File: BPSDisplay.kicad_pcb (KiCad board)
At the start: 2 copper layers, 45 parts, among them J1 SWD, J2 Conn_02x06_Counter_Clockwise, P1 Conn_02x20_Odd_Even, SW1 Reset, U1 STM32F413RHTx, U7 NCP1117-3.3_SOT223, Y1 8M

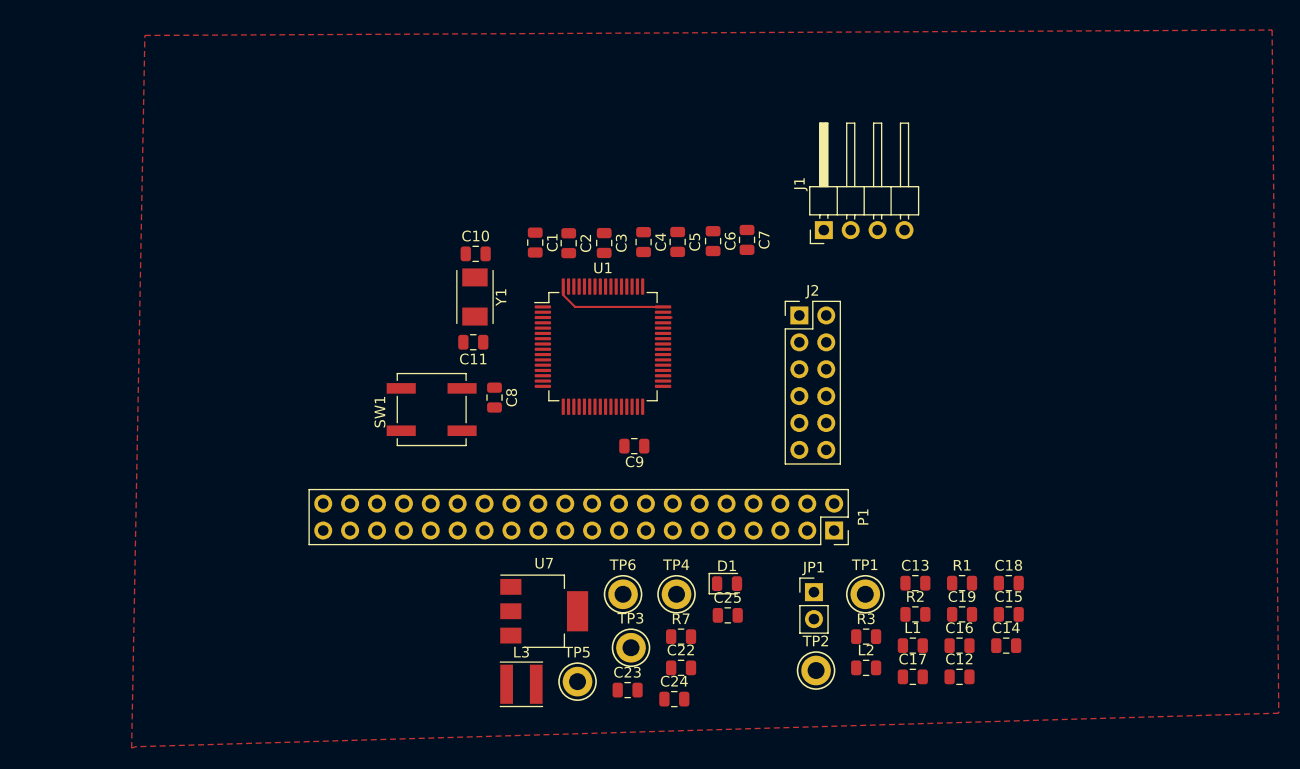
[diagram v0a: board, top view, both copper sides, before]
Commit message: Rearranging PCB layout
Power distribution circuit is laid out, CAN interface is done using the recommended PCB layout, and all the mounting holes and connectors are in the same places as they were in the old board.
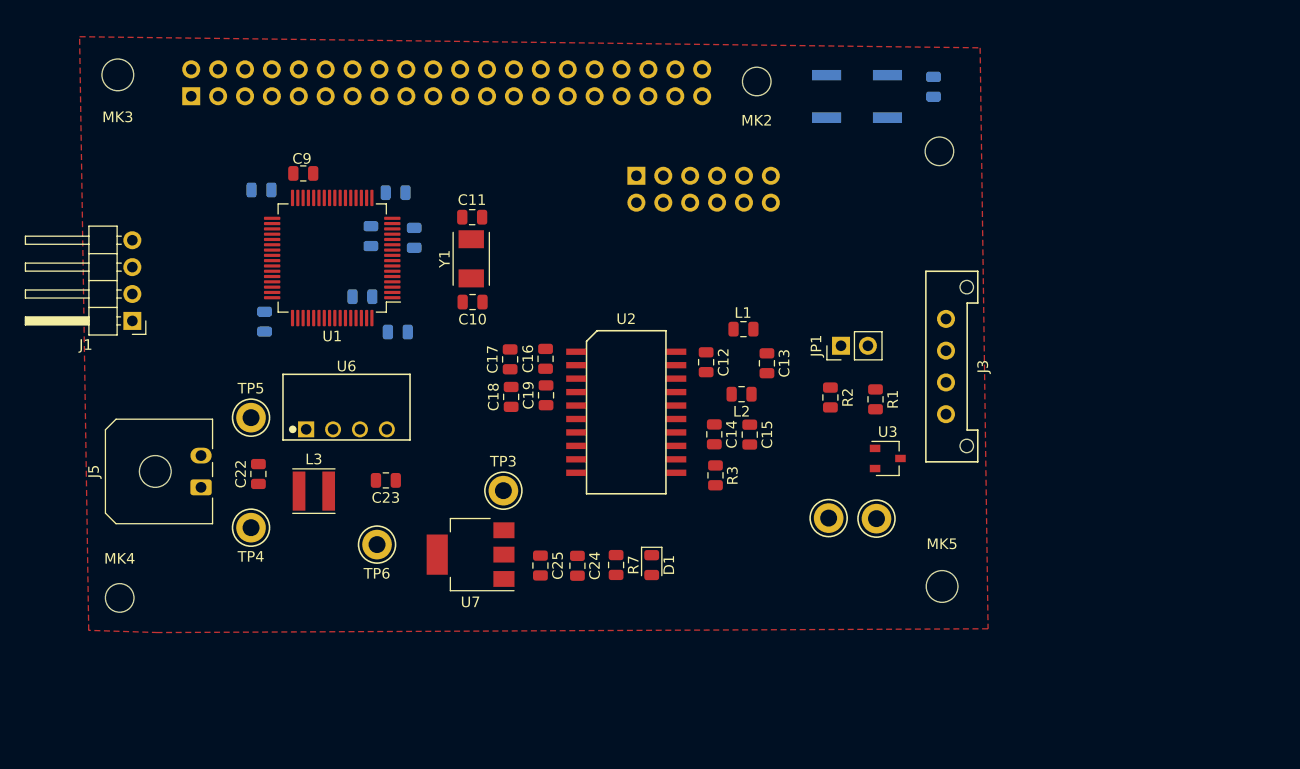
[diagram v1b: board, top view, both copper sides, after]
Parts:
- added J3: CAN_Out, UTSVT_Connectors:Molex_MicroFit3.0_1x4xP3.00mm_PolarizingPeg_Vertical, F.Cu at (278.0, 131.9)
- added J5: CarPowerConnector, Connector_Molex:Molex_Micro-Fit_3.0_43650-0200_1x02_P3.00mm_Horizontal, F.Cu at (207.6, 147.8)
- added MK1: M2.5, MountingHole:MountingHole_2.7mm_M2.5, F.Cu at (277.3, 116.0)
- added MK2: M2.5, MountingHole:MountingHole_2.7mm_M2.5, F.Cu at (260.1, 109.4)
- added MK3: M3, MountingHole:MountingHole_3mm, F.Cu at (199.7, 108.8)
- added MK4: M2.5, MountingHole:MountingHole_2.7mm_M2.5, F.Cu at (199.9, 158.2)
- added MK5: M3, MountingHole:MountingHole_3mm, F.Cu at (277.6, 157.1)
- added U2: ADM3055E, UTSVT_ICs:SOIC-20W_7.5x15.4mm_Pitch1.27mm, F.Cu at (247.8, 140.7)
- added U3: CDSOT23-T24CAN, Package_TO_SOT_SMD:SOT-23W, F.Cu at (272.5, 145.0)
- added U6: PDS1-S12-S5, UTSVT_ICs:PDSx-S, F.Cu at (221.3, 142.3)
- C1, C2, C3, C4, C5, C6, C7, C8, J2, P1, SW1: moved to B.Cu
- moved P1 73.3 mm to (206.7, 110.8)
- moved J1 65.9 mm to (201.1, 132.0), turned to 180 degrees
- moved C8 50.8 mm to (276.8, 109.9), turned to 90 degrees
- moved C18 50.2 mm to (236.9, 139.2), turned to 90 degrees
- moved SW1 49.9 mm to (269.6, 110.8)
- moved C17 48.4 mm to (236.8, 135.7), turned to 90 degrees
- moved C16 47.6 mm to (240.1, 135.6), turned to 90 degrees
- moved C19 44.4 mm to (240.2, 139.1), turned to 90 degrees
- moved C22 43.9 mm to (213.0, 146.5), turned to 90 degrees
- moved TP4 40.7 mm to (212.3, 151.6), turned to 180 degrees
- moved C9 40.5 mm to (217.2, 118.1), turned to 180 degrees
- moved TP5 39.7 mm to (212.3, 141.2)
- moved C12 38.2 mm to (255.3, 136.0), turned to 270 degrees
- moved C4 36.6 mm to (213.6, 132.1), turned to 90 degrees
- moved C7 35.5 mm to (223.6, 124.0)
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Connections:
- net /DISPCS renamed Net-(U1-Pad50)
- net /GPIO12(PWM0) renamed Net-(P1-Pad32)
- net /GPIO14(TXD0) renamed Net-(P1-Pad8)
- net /GPIO15(RXD0) renamed Net-(P1-Pad10)
- net /GPIO16 renamed Net-(P1-Pad36)
- net /GPIO18(GEN1)(PWM0) renamed Net-(P1-Pad12)
- net /GPIO2(SDA1) renamed Net-(P1-Pad3)
- net /GPIO20(SPI1_MOSI) renamed Net-(P1-Pad38)
- net /GPIO21(SPI1_SCK) renamed Net-(P1-Pad40)
- net /GPIO22(GEN3) renamed Net-(P1-Pad15)
- net /GPIO23(GEN4) renamed Net-(P1-Pad16)
- net /GPIO26 renamed Net-(P1-Pad37)
- net /GPIO27(GEN2) renamed Net-(P1-Pad13)
- net /GPIO3(SCL1) renamed Net-(P1-Pad5)
- net /GPIO4(GCLK) renamed Net-(P1-Pad7)
- net /GPIO7(SPI1_CE_N) renamed Net-(P1-Pad26)
- net /ID_SC renamed Net-(P1-Pad28)
- net /ID_SD renamed Net-(P1-Pad27)
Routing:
- net +3V3: track 10.7 -> 0.00 mm
- net /SWDIO: track 0.81 -> 0.00 mm

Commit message: Added traces
We added some preliminary traces to the PCB. There are a few pins that are still unconnected.
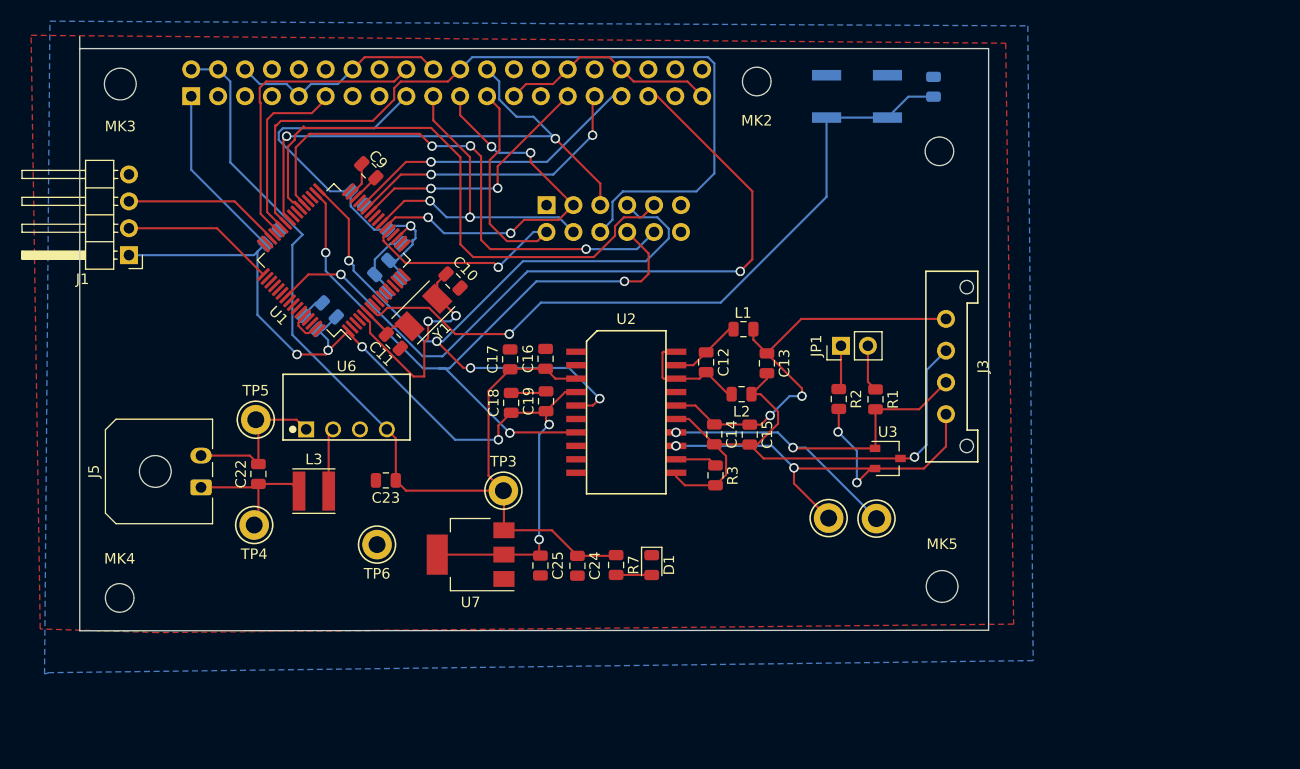
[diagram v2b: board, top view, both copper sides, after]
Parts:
- moved C11 13.9 mm to (225.7, 134.0), turned to 315 degrees
- moved C3 9.12 mm to (222.4, 120.5), turned to 315 degrees
- moved J2 8.93 mm to (240.2, 121.1)
- moved C2 8.31 mm to (217.9, 132.2), turned to 135 degrees
- moved C4 8.05 mm to (214.3, 124.1), turned to 45 degrees
- moved Y1 6.80 mm to (228.6, 131.3), turned to 225 degrees
- moved J1 6.22 mm to (200.8, 125.8)
- moved C9 6.20 mm to (223.4, 117.9), turned to 135 degrees
- moved C6 4.86 mm to (225.8, 128.6), turned to 225 degrees
- moved C1 4.16 mm to (225.9, 124.1), turned to 315 degrees
- moved C5 3.37 mm to (219.7, 131.0), turned to 135 degrees
- moved C7 3.13 mm to (224.7, 127.0), turned to 225 degrees
- moved C10 2.71 mm to (231.4, 128.3), turned to 315 degrees
- moved MK3 0.90 mm to (200.0, 109.7)
- moved R2 0.80 mm to (267.8, 139.4)
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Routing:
- net +3V3: track 0.00 -> 144.7 mm, vias 0 -> 7
- net +5V: track 0.00 -> 94.6 mm
- net /GPIO25(GEN6): track 0.00 -> 79.1 mm
- net /GPIO19: track 0.00 -> 71.9 mm, vias 0 -> 2
- net /CAN2_RX: track 0.00 -> 71.4 mm, vias 0 -> 4
- net /NRST: track 0.00 -> 68.4 mm, vias 0 -> 1
- net /CAN2_TX: track 0.00 -> 66.0 mm, vias 0 -> 3
- net GND: track 0.00 -> 60.5 mm
- net /USART6_RX: track 0.00 -> 55.4 mm
- net Net-(C13-Pad2): track 0.00 -> 55.0 mm, vias 0 -> 1
- net /GPIO8(SPI0_CE_N): track 0.00 -> 52.0 mm, vias 0 -> 2
- net /USART6_TX: track 0.00 -> 49.9 mm, vias 0 -> 3
- net /CAN/CAN_L: track 0.00 -> 46.4 mm, vias 0 -> 4
- net /CAN/CAN_H: track 0.00 -> 41.5 mm, vias 0 -> 2
- net Net-(C13-Pad1): track 0.00 -> 40.3 mm, vias 0 -> 2
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- added copper zone on B.Cu, net GND
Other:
- board outline added: 85.9 x 56.1 mm

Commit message: Completed Traces and resized to correct dim.
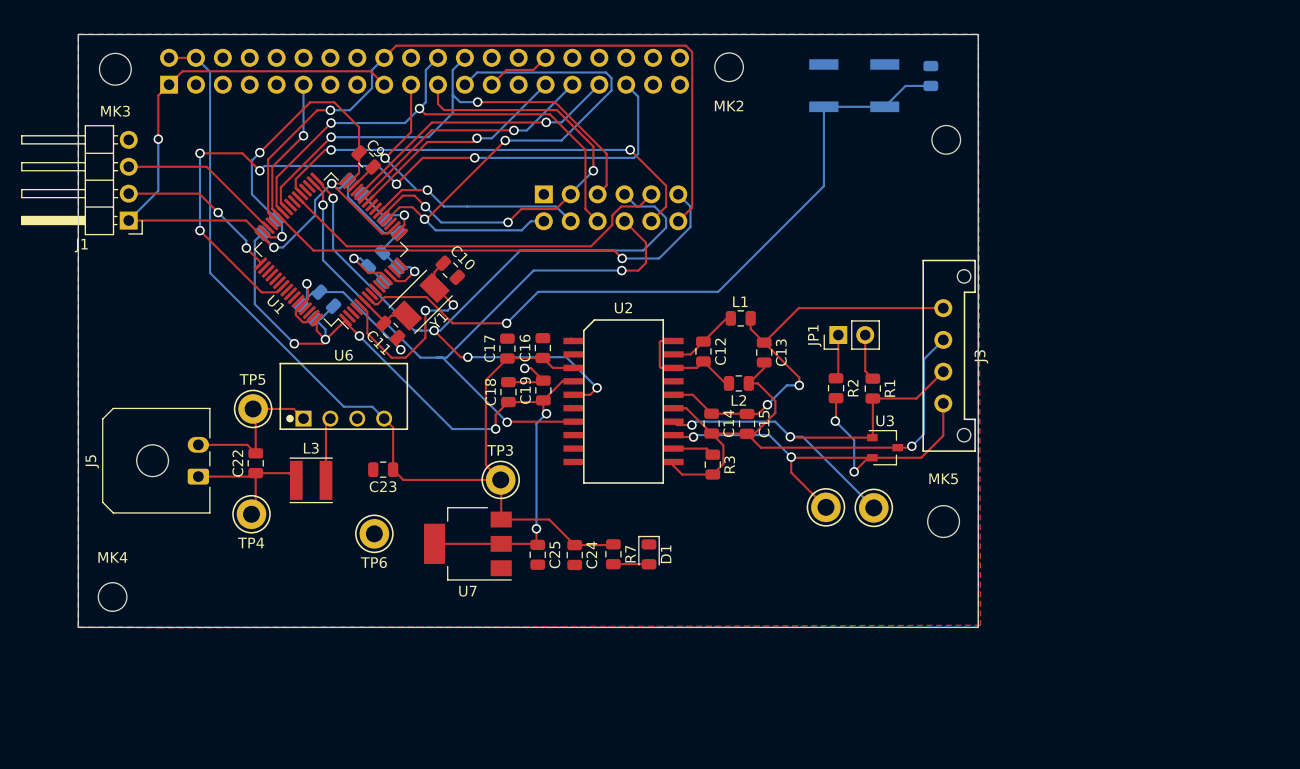
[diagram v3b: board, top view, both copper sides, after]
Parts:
- moved MK5 6.13 mm to (277.7, 151.0)
- moved J1 3.27 mm to (200.8, 122.6)
- moved MK2 2.94 mm to (257.5, 108.1)
- moved P1 2.36 mm to (204.6, 109.7)
- moved MK3 1.47 mm to (199.5, 108.3)
- moved MK1 1.26 mm to (278.0, 114.9)
- moved C2 1.05 mm to (217.7, 131.2)
- moved C5 1.05 mm to (219.5, 130.0)
- moved R2 1.05 mm to (267.6, 138.4)
- moved C12 1.05 mm to (255.0, 134.9)
- moved C17 1.05 mm to (236.5, 134.7)
- moved C18 1.05 mm to (236.6, 138.8)
- moved C19 1.05 mm to (239.9, 138.6)
- moved C23 1.05 mm to (224.8, 146.1)
- moved C25 1.05 mm to (239.4, 154.1)
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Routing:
- net /GPIO17(GEN0): track 17.4 -> 60.9 mm, vias 0 -> 2
- net /GPIO24(GEN5): track 28.8 -> 69.2 mm, vias 0 -> 1
- net /GPIO25(GEN6): track 79.1 -> 49.8 mm, vias 0 -> 2
- net +3V3: track 144.7 -> 167.3 mm, vias 7 -> 10
- net /USART6_RX: track 55.4 -> 37.9 mm
- net GND: track 60.5 -> 77.3 mm, vias 0 -> 7
- net /GPIO11(SPI0_SCK): track 38.3 -> 55.0 mm, vias 1 -> 2
- net /GPIO9(SPI0_MISO): track 36.4 -> 44.3 mm, vias 4 -> 3
- net /USART6_TX: track 49.9 -> 43.1 mm, vias 3 -> 2
- net /GPIO8(SPI0_CE_N): track 52.0 -> 48.1 mm
- net /GPIO6: track 27.9 -> 24.1 mm, vias 2 -> 1
- net /GPIO5: track 24.3 -> 21.3 mm, vias 2 -> 1
- net /GPIO19: track 71.9 -> 69.0 mm, vias 2 -> 5
- net /GPIO13: track 28.6 -> 26.8 mm
- net +5V: track 94.6 -> 96.2 mm
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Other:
- board size 85.9 x 56.1 mm -> 85 x 56 mm

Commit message: Added Labels
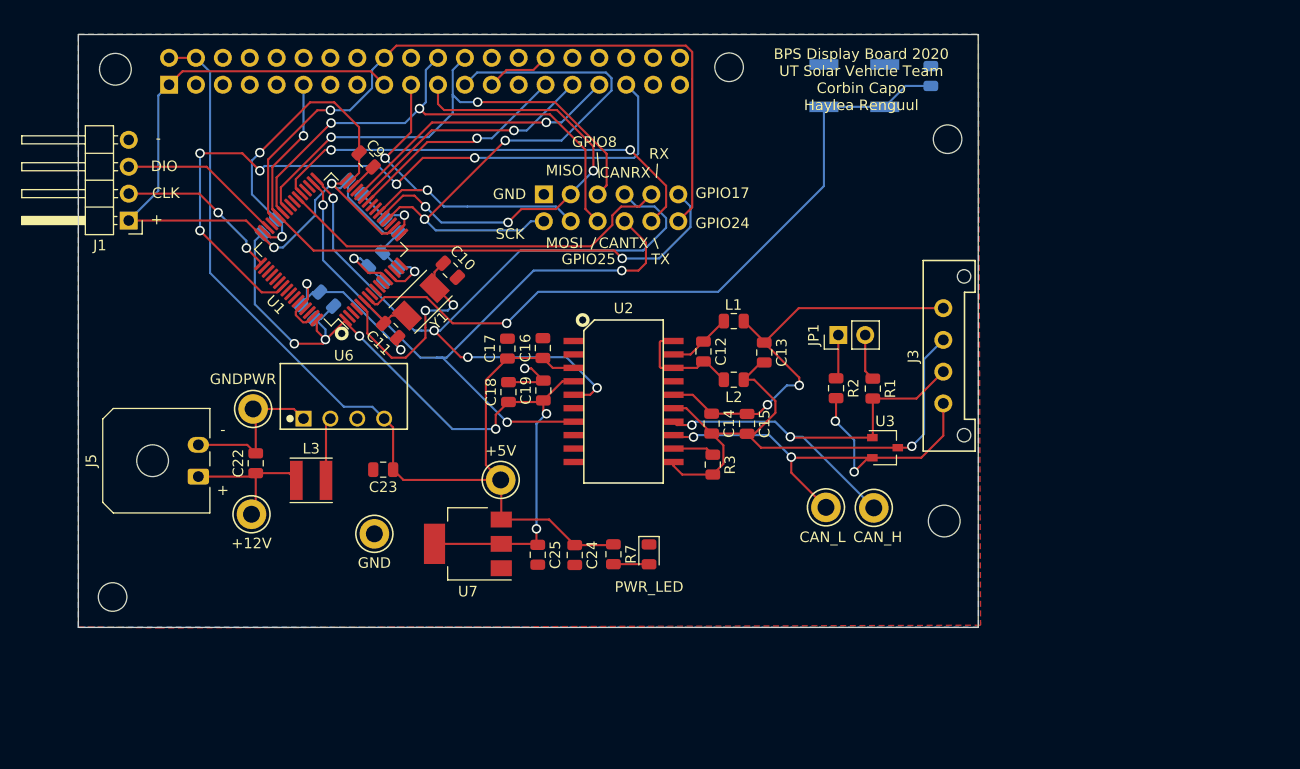
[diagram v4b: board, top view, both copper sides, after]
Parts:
- moved L1 0.71 mm to (257.9, 132.1)
- moved L2 0.59 mm to (257.9, 137.6)
- moved MK1 0.14 mm to (278.1, 114.9)
- moved MK5 0.08 mm to (277.8, 151.0)
- renumbered TP4 to +12V, TP3 to +5V, TP1 to CAN_H, TP2 to CAN_L, TP6 to GND, TP5 to GNDPWR, D1 to PWR_LED
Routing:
- net Net-(C12-Pad1): track 6.84 -> 6.08 mm
- net Net-(C13-Pad2): track 55.0 -> 55.6 mm
- net Net-(C12-Pad2): track 11.3 -> 10.7 mm
- net +3V3: vias 10 -> 9
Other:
- board text added: "+"
- board text added: "-"
- board text added: "BPS Display Board 2020 UT Solar Vehicle Team Corbin Capo Haylea Renguul"
- board text added: "CANRX"
- board text added: "CANTX"
- board text added: "CLK"
- board text added: "DIO"
- board text added: "GND"
- board text added: "GPIO17"
- board text added: "GPIO24"
- board text added: "GPIO25"
- board text added: "GPIO8"
- board text added: "MISO"
- board text added: "MOSI"
- board text added: "RESET"
- board text added: "RX"
- board text added: "SCK"
- board text added: "TX"

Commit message: Edits to PCB layout
Rounded out corners of the board, added pin labels to connectors, rearranged trace that was too close to U1
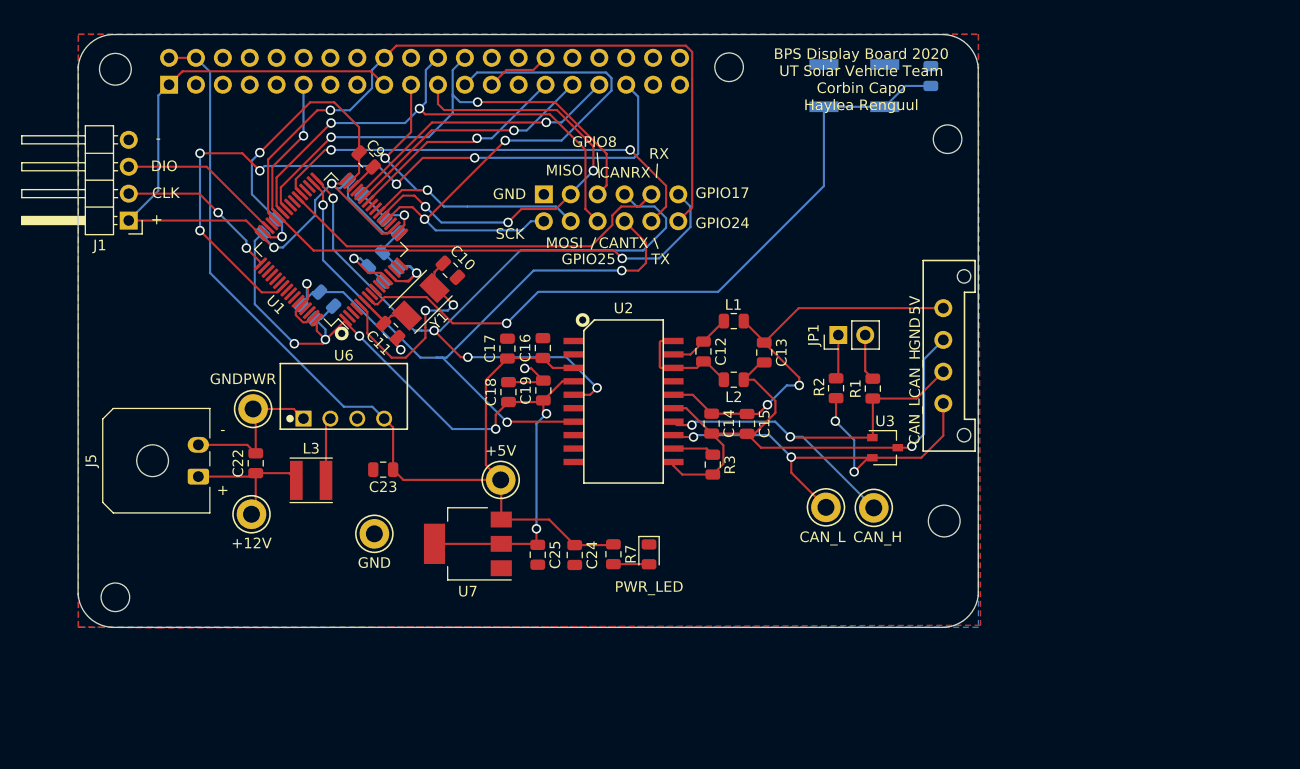
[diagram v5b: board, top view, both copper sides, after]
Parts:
- moved MK4 0.26 mm to (199.5, 158.2)
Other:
- outline, holes or cut-outs redrawn
- board text added: "5V"
- board text added: "CAN_H"
- board text added: "CAN_L"
